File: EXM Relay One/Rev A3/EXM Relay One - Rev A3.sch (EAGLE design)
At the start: 9 parts, among them J1 MSTBA2, J2 MSTBA3, J3 22-05-7038-03, J4 22-05-7038-03, K1 MY2, T1 EXMACHINA-LOGO-NAME

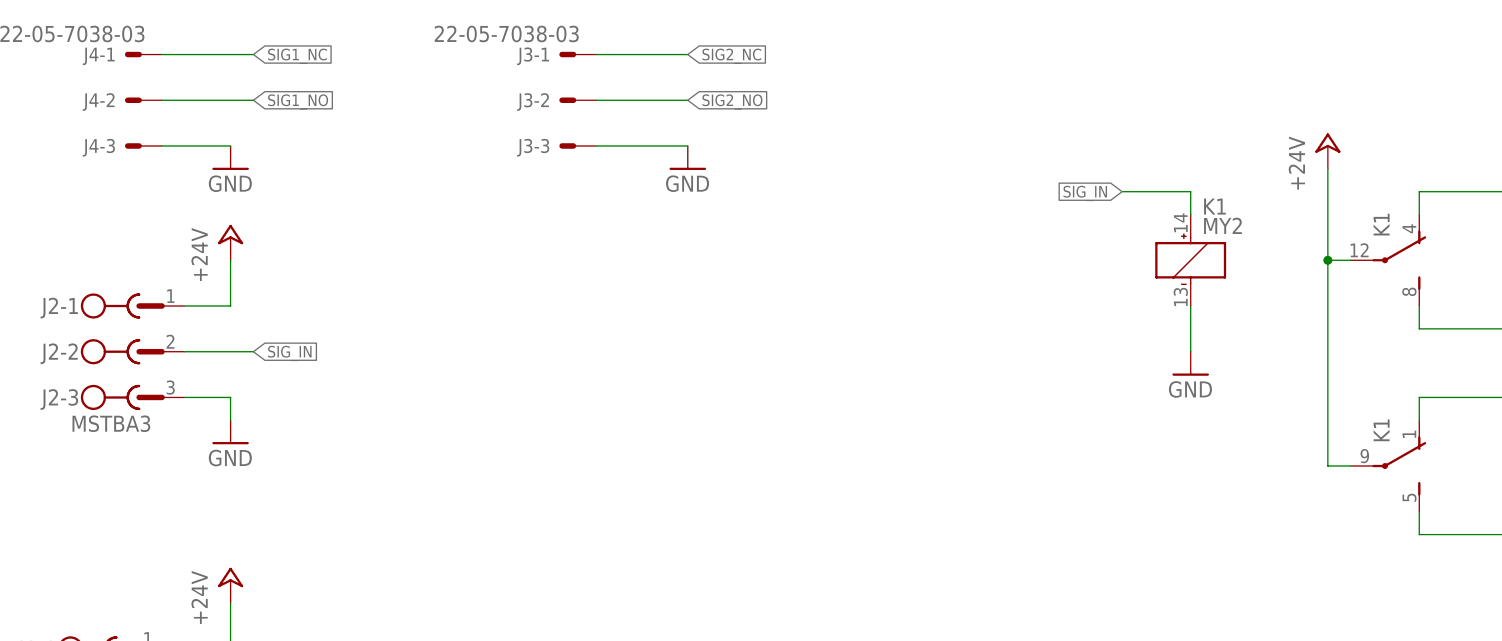
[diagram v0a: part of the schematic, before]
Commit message: Add EXM Relay One rev A3
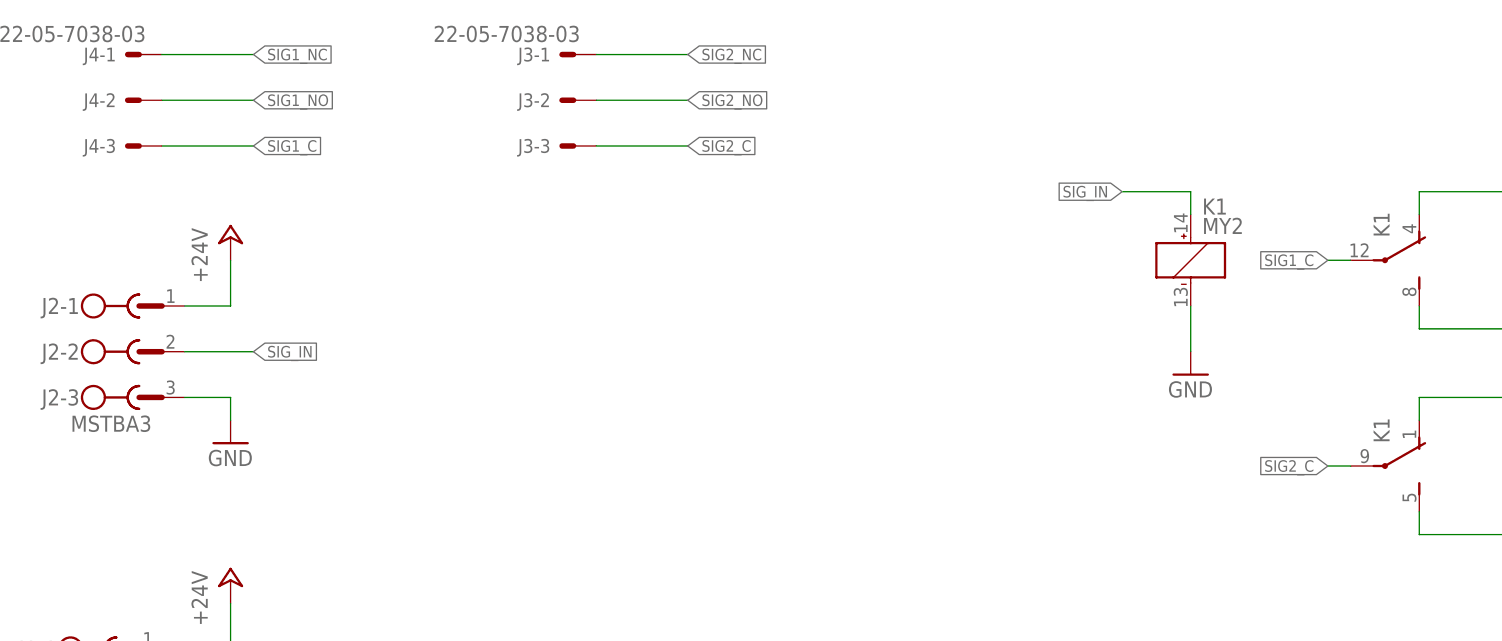
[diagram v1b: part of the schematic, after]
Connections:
- new net SIG1_C: J4-3.S, K1G$2.C
- new net SIG2_C: J3-3.S, K1G$3.C
- net +24V: no longer K1G$2.C, K1G$3.C
- net GND: no longer J3-3.S, J4-3.S
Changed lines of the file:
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@@
 <part name="P+1" library="supply3" deviceset="+24V" device=""/>
 <part name="GND1" library="supply3" deviceset="GND" device=""/>
-<part name="GND2" library="supply3" deviceset="GND" device=""/>
 <part name="GND3" library="supply3" deviceset="GND" device=""/>
-<part name="P+2" library="supply3" deviceset="+24V" device=""/>
 <part name="CC1" library="cc-by-sa" deviceset="CC-BY-NC-SA" device=""/>
 <part name="T1" library="exmachina" deviceset="EXMACHINA-LOGO" device="-NAME"/>
@@
 <part name="J4" library="con-molex" deviceset="22-?-03" device="05-7038"/>
 <part name="J3" library="con-molex" deviceset="22-?-03" device="05-7038"/>
-<part name="GND5" library="supply3" deviceset="GND" device=""/>
 </parts>
 <sheets>
@@
 <instance part="P+1" gate="1" x="35.56" y="220.98"/>
 <instance part="GND1" gate="1" x="35.56" y="198.12"/>
-<instance part="GND2" gate="1" x="35.56" y="228.6"/>
 <instance part="GND3" gate="1" x="142.24" y="205.74"/>
-<instance part="P+2" gate="1" x="157.48" y="231.14"/>
 <instance part="CC1" gate="G$1" x="304.8" y="10.16"/>
 <instance part="T1" gate="G$1" x="312.42" y="20.32"/>
@@
 <instance part="J3" gate="-2" x="73.66" y="236.22" rot="MR0"/>
 <instance part="J3" gate="-3" x="73.66" y="231.14" rot="MR0"/>
-<instance part="GND5" gate="1" x="86.36" y="228.6"/>
 <instance part="K1" gate="G$1" x="142.24" y="218.44"/>
 </instances>
@@
 <wire x1="30.48" y1="213.36" x2="35.56" y2="213.36" width="0.1524" layer="91"/>
 <wire x1="35.56" y1="213.36" x2="35.56" y2="218.44" width="0.1524" layer="91"/>
-</segment>
-<segment>
-<pinref part="K1" gate="G$2" pin="C"/>
-<pinref part="P+2" gate="1" pin="+24V"/>
-<wire x1="160.02" y1="218.44" x2="157.48" y2="218.44" width="0.1524" layer="91"/>
-<wire x1="157.48" y1="218.44" x2="157.48" y2="228.6" width="0.1524" layer="91"/>
-<pinref part="K1" gate="G$3" pin="C"/>
-<wire x1="160.02" y1="195.58" x2="157.48" y2="195.58" width="0.1524" layer="91"/>
-<wire x1="157.48" y1="195.58" x2="157.48" y2="218.44" width="0.1524" layer="91"/>
-<junction x="157.48" y="218.44"/>
 </segment>
 <segment>
@@
 </segment>
 <segment>
-<pinref part="GND2" gate="1" pin="GND"/>
-<wire x1="27.94" y1="231.14" x2="35.56" y2="231.14" width="0.1524" layer="91"/>
-<pinref part="J4" gate="-3" pin="S"/>
-</segment>
-<segment>
 <pinref part="GND3" gate="1" pin="GND"/>
 <wire x1="142.24" y1="213.36" x2="142.24" y2="208.28" width="0.1524" layer="91"/>
@@
 <wire x1="27.94" y1="170.18" x2="35.56" y2="170.18" width="0.1524" layer="91"/>
 <wire x1="35.56" y1="170.18" x2="35.56" y2="167.64" width="0.1524" layer="91"/>
-</segment>
-<segment>
-<pinref part="J3" gate="-3" pin="S"/>
-<wire x1="76.2" y1="231.14" x2="86.36" y2="231.14" width="0.1524" layer="91"/>
-<pinref part="GND5" gate="1" pin="GND"/>
 </segment>
 </net>
@@
 </segment>
 </net>
+<net name="SIG2_C" class="0">
+<segment>
+<pinref part="J3" gate="-3" pin="S"/>
+<wire x1="76.2" y1="231.14" x2="86.36" y2="231.14" width="0.1524" layer="91"/>
+<label x="86.36" y="231.14" size="1.27" layer="95" xref="yes"/>
+</segment>
+<segment>
+<pinref part="K1" gate="G$3" pin="C"/>
+<wire x1="160.02" y1="195.58" x2="157.48" y2="195.58" width="0.1524" layer="91"/>
+<label x="157.48" y="195.58" size="1.27" layer="95" rot="R180" xref="yes"/>
+</segment>
+</net>
+<net name="SIG1_C" class="0">
+<segment>
+<pinref part="J4" gate="-3" pin="S"/>
+<wire x1="27.94" y1="231.14" x2="38.1" y2="231.14" width="0.1524" layer="91"/>
+<label x="38.1" y="231.14" size="1.27" layer="95" xref="yes"/>
+</segment>
+<segment>
+<pinref part="K1" gate="G$2" pin="C"/>
+<wire x1="160.02" y1="218.44" x2="157.48" y2="218.44" width="0.1524" layer="91"/>
+<label x="157.48" y="218.44" size="1.27" layer="95" rot="R180" xref="yes"/>
+</segment>
+</net>
